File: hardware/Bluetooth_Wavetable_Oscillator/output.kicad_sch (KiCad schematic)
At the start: 13 parts, among them J2 AudioJack2, U6 NE5532

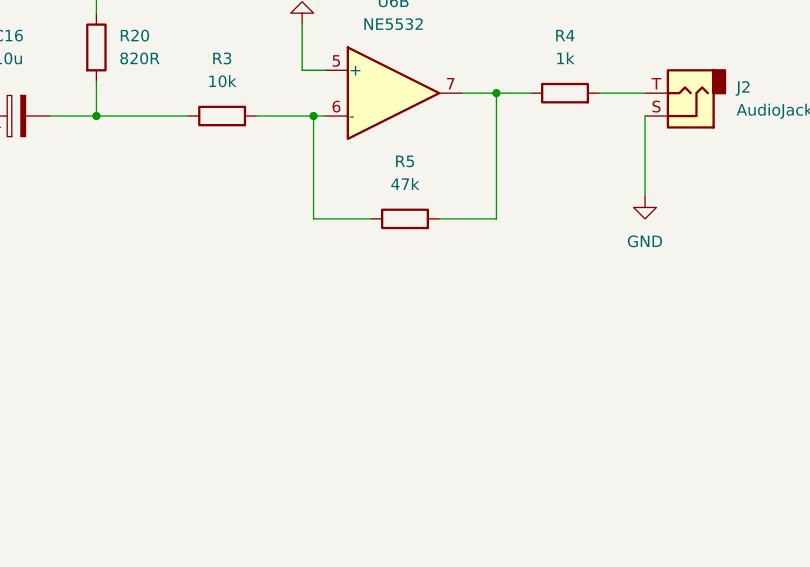
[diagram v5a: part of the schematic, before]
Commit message: add feedback capacitor
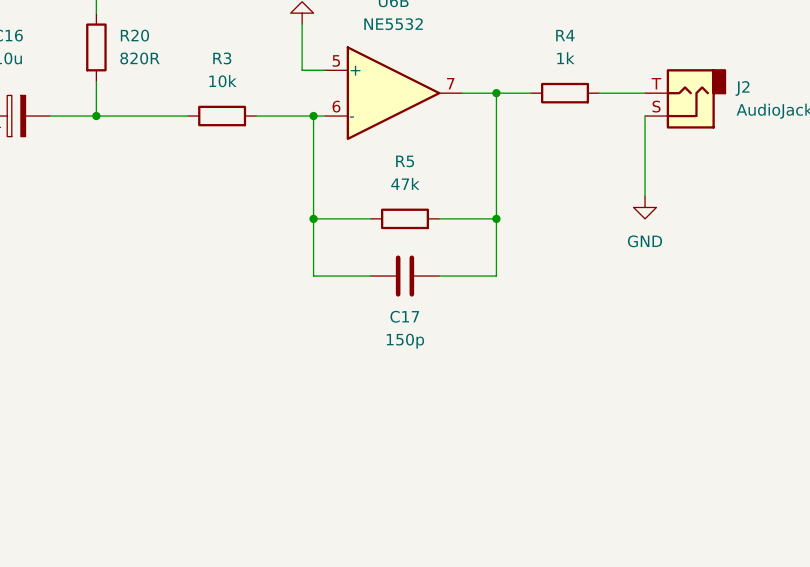
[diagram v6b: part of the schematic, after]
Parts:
- added C17: 150p, symbol Device:C
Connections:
- net at R3.2, R5.1, U6.6 (-): now also C17.2
- net at R4.1, R5.2, U6.7: now also C17.1
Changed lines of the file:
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@@
 	(title_block
 		(title "Output")
-		(date "2024-11-18")
+		(date "2025-01-03")
 		(rev "1")
 	)
@@
 	)
 	(junction
+		(at 193.04 109.22)
+		(diameter 0)
+		(color 0 0 0 0)
+	)
+	(junction
+		(at 172.72 109.22)
+		(diameter 0)
+		(color 0 0 0 0)
+	)
+	(junction
 		(at 87.63 95.25)
 		(diameter 0)
@@
 	(wire
 		(pts
+			(xy 193.04 115.57) (xy 193.04 109.22)
+		)
+		(stroke
+			(width 0)
+			(type default)
+		)
+	)
+	(wire
+		(pts
 			(xy 189.23 95.25) (xy 193.04 95.25)
 		)
@@
 	(wire
 		(pts
+			(xy 179.07 115.57) (xy 172.72 115.57)
+		)
+		(stroke
+			(width 0)
+			(type default)
+		)
+	)
+	(wire
+		(pts
 			(xy 148.59 93.98) (xy 148.59 97.79)
 		)
@@
 	(wire
 		(pts
+			(xy 186.69 115.57) (xy 193.04 115.57)
+		)
+		(stroke
+			(width 0)
+			(type default)
+		)
+	)
+	(wire
+		(pts
 			(xy 101.6 95.25) (xy 101.6 99.06)
 		)
@@
 		(pts
 			(xy 148.59 97.79) (xy 158.75 97.79)
+		)
+		(stroke
+			(width 0)
+			(type default)
+		)
+	)
+	(wire
+		(pts
+			(xy 172.72 115.57) (xy 172.72 109.22)
 		)
 		(stroke
@@
 					(unit 1)
 				)
+			)
+		)
+	)
+	(symbol
+		(lib_id "Device:C")
+		(at 182.88 115.57 270)
+		(unit 1)
+		(exclude_from_sim no)
+		(in_bom yes)
+		(on_board yes)
+		(dnp no)
+		(property "Reference" "C17"
+			(at 182.88 120.142 90)
+			(effects
+				(font
+					(size 1.27 1.27)
+				)
+			)
+		)
+		(property "Value" "150p"
+			(at 182.88 122.682 90)
+			(effects
+				(font
+					(size 1.27 1.27)
+				)
+			)
+		)
+		(property "Footprint" ""
+			(at 179.07 116.5352 0)
+			(effects
+				(font
+					(size 1.27 1.27)
+				)
+				(hide yes)
+			)
+		)
+		(property "Datasheet" "~"
+			(at 182.88 115.57 0)
+			(effects
+				(font
+					(size 1.27 1.27)
+				)
+				(hide yes)
+			)
+		)
+		(property "Description" "Unpolarized capacitor"
+			(at 182.88 115.57 0)
+			(effects
+				(font
+					(size 1.27 1.27)
+				)
+				(hide yes)
+			)
+		)
+		(pin "2"
+		)
+		(pin "1"
+		)
+		(instances
+			(project ""
+				(path "/fda99055-d953-4203-b673-64a5e6540552/e721cc72-9f0b-4653-9ded-ede3b48f082c"
+					(reference "C17")
+					(unit 1)
+				)
